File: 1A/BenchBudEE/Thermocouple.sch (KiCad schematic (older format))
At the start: 0 parts

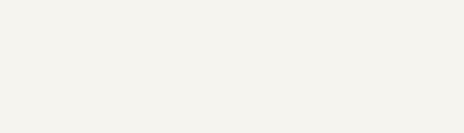
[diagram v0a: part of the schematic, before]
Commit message: Define component inputs and outputs
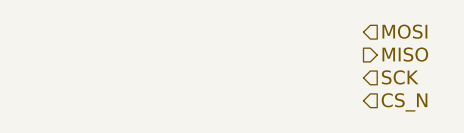
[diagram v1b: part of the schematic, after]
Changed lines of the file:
@@
 Text HLabel 1300 1000 0    60   Input ~ 0
 TC IN +
+Text HLabel 10700 800  2    60   Input ~ 0
+MOSI
+Text HLabel 10700 900  2    60   Output ~ 0
+MISO
+Text HLabel 10700 1000 2    60   Input ~ 0
+SCK
+Text HLabel 10700 1100 2    60   Input ~ 0
+CS_N
 $EndSCHEMATC
